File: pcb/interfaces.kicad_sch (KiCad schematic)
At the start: 12 parts

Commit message: Fixed LCSC part numbers and attributes
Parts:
- J1: MPN BM04B-SRSS-TBT(LF)(SN) -> SM04B-SRSS-TBT(LF)(SN)
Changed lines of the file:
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@@
 			)
 		)
-		(property "MPN" "BM04B-SRSS-TBT(LF)(SN)"
+		(property "MPN" "SM04B-SRSS-TBT(LF)(SN)"
 			(at 35.052 54.356 0)
 			(effects

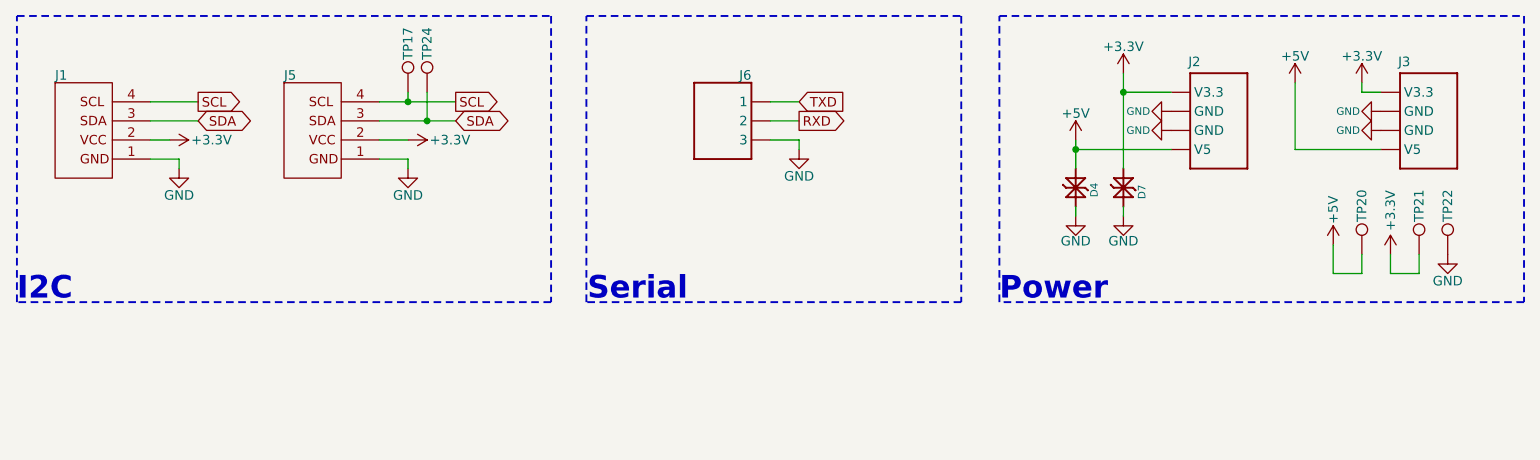
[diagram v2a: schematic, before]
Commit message: Updates for consistency
Changed mounting holes to grounded
Updated power connectors
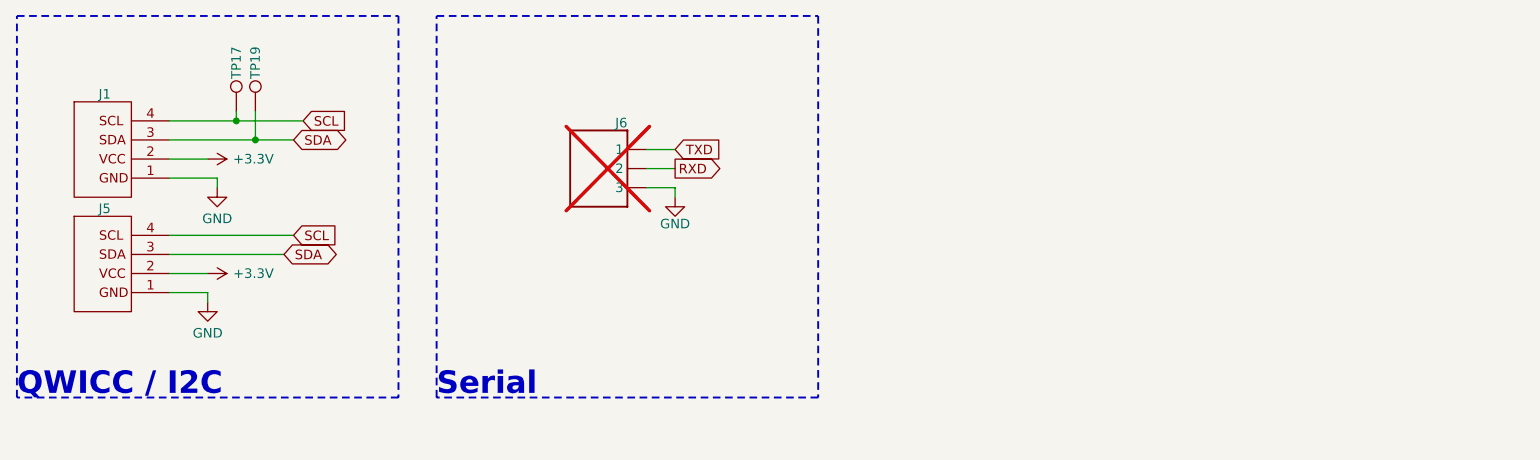
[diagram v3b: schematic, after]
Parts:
- removed D4: PESD5V5C1BL, CRGM Passive:DFN1006-2, symbol CRGM Passive:PESD5V5C1BLYL
- removed D7: PESD3V3S1BL, CRGM Passive:DFN1006-2, symbol CRGM Passive:PESD3V3S1BL
- removed J2, J3: ~, CRGM Connector:JST_SH_SM04B-SRSS-TB_1x04-1MP_P1.00mm_Horizontal, symbol CRGM Connector:AQ_POWER
- removed TP17, TP20, TP21, TP22, TP24: ~, CRGM Mechanical:TestPoint_Pad_D1.0mm, symbol Connector:TestPoint
- added TP17, TP19: ~, CRGM Mechanical:TestPoint_Pad_D1.0mm, symbol CRGM Connector:TestPoint
- J1: Digikey 455-BM04B-SRSS-TBTR-ND -> 455-SM04B-SRSS-TBTR-ND; Mouser 306-BM04BSRSSTBTLFSN -> 306-SM04BSRSSTBTLFSN
- J6: now not fitted; now left out of the parts list
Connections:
- net SCL: now also TP17.1
- net SDA: now also TP19.1
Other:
- note added: "QWICC / I2C"
- note removed: "I2C"
- note removed: "Power"

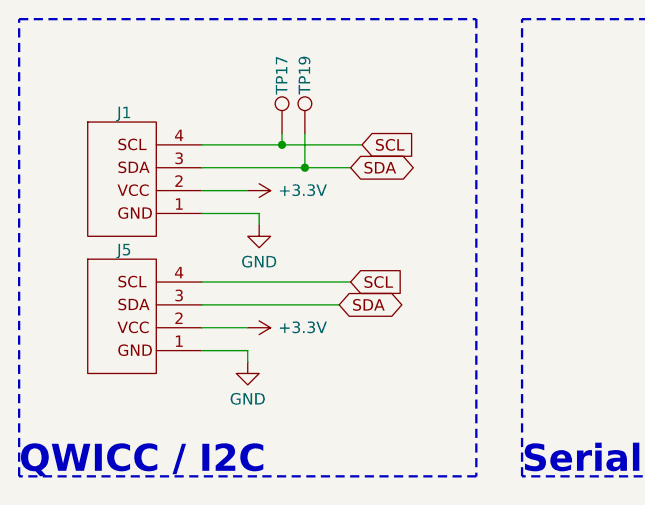
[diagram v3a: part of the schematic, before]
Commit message: Removed power connectors
Removed power connector as 5v is not necessary.
Added 100uF caps to power
Added TVS to I2C and VOUT
Rerouted entire board
Adjusted silkscreen
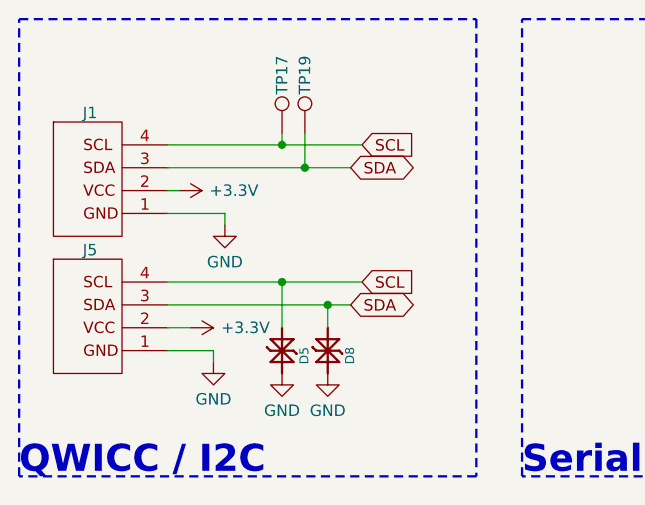
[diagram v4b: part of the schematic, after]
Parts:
- added D5, D8: PESD3V3S1BL, CRGM Passive:DFN1006-2, symbol CRGM Passive:PESD3V3S1BL
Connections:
- net GND: now also D5.1 (K1), D8.1 (K1)
- net SCL: now also D5.2 (K2)
- net SDA: now also D8.2 (K2)
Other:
- moved on the sheet: J1, J5

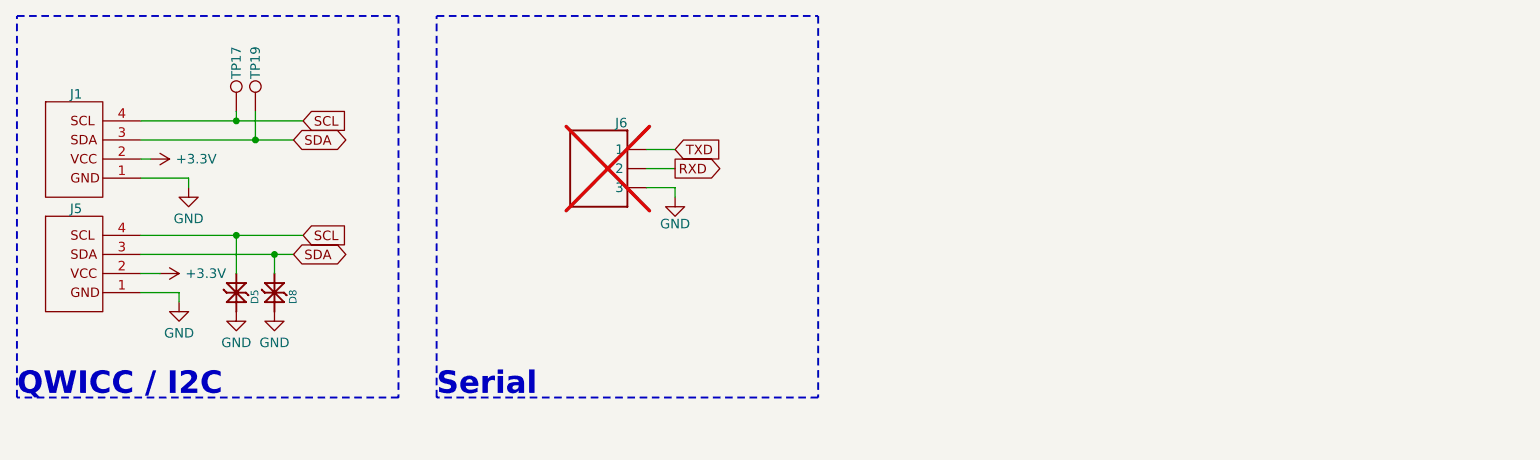
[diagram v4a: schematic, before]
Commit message: Collapsed UPDI and Serial
Added indicator LEDs
Rerouted
Cleaned up silkscreen
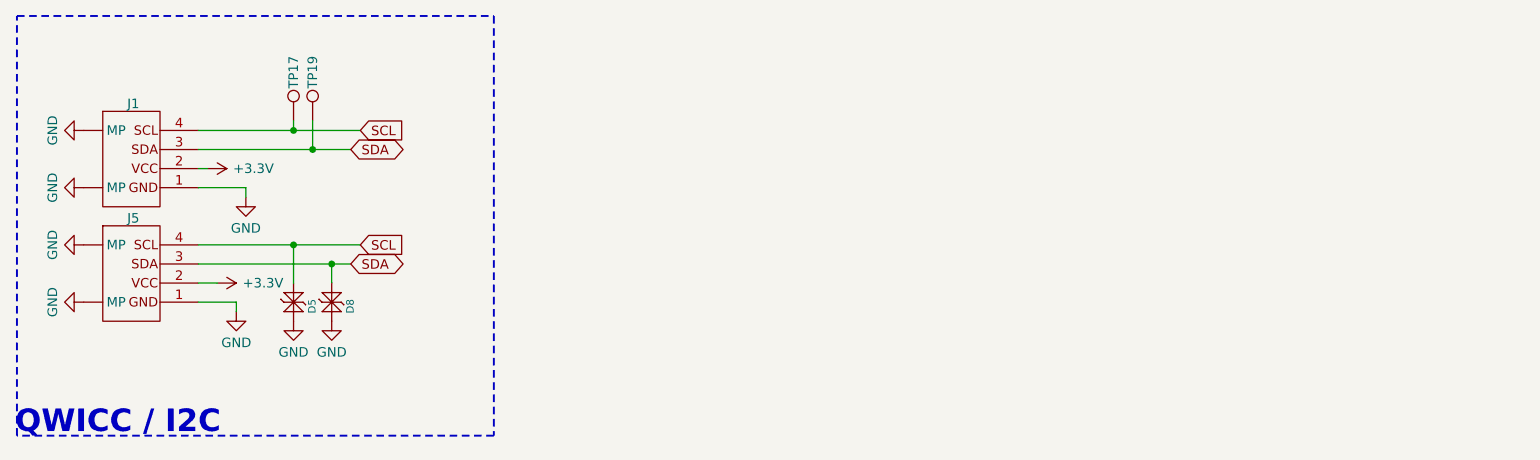
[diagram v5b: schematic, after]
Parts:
- removed J6: ~, CRGM Connector:JST_SH_BM03B-SRSS-TB_1x03-1MP_P1.00mm_Vertical, symbol CRGM Connector:JST-SH-3
- J1, J5: footprint CRGM Connector:JST_SH_SM04B-SRSS-TB_1x04-1MP_P1.00mm_Horizontal -> CRGM Connector:JST_SH_BM04B-SRSS-TB_1x04-1MP_P1.00mm_Vertical; Digikey 455-SM04B-SRSS-TBTR-ND -> 455-BM04B-SRSS-TBTR-ND; LCSC C2763614 -> C2919601; MPN SM04B-SRSS-TBT(LF)(SN) -> BM04B-SRSS-TBT(LF)(SN); Mouser 306-SM04BSRSSTBTLFSN -> 306-BM04BSRSSTBTLFSN
- TP17, TP19: now left out of the parts list
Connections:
- net GND: now also J1.0 (MP), J1.5 (MP), J5.0 (MP), J5.5 (MP)
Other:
- note removed: "Serial"
- moved on the sheet: D5, D8, TP17, TP19
